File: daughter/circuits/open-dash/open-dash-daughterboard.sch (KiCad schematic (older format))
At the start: 13 parts, among them J1 Conn_01x01_Female, J2 Conn_01x01_Female, J3 Conn_01x01_Female, J4 Conn_01x01_Female, J43 Conn_02x02_Counter_Clockwise, J5 Conn_02x06_Odd_Even, J6 Conn_IDE_40, J7 Conn_IDE_40, J8 Conn_IDE_40, Q40 Q_AO3401A

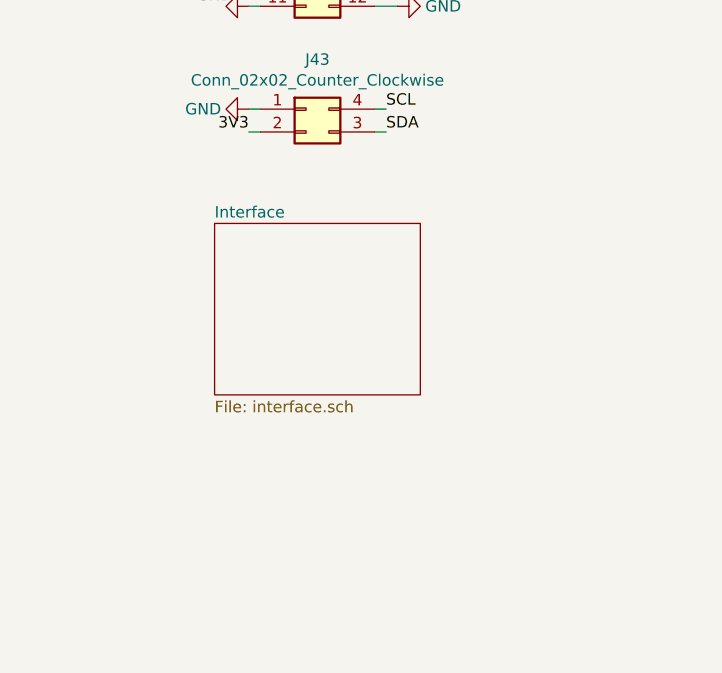
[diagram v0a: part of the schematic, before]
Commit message: send v1.4 to board house. Corrected source-drain on fets.
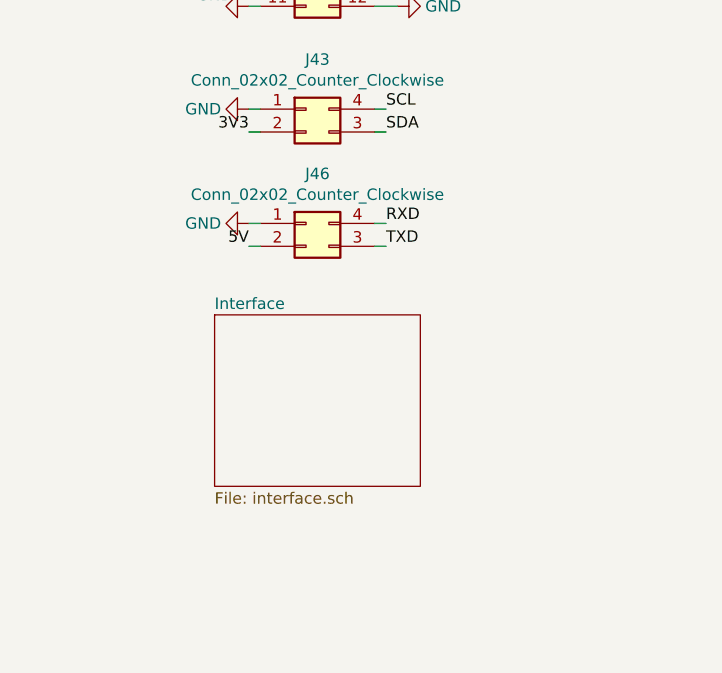
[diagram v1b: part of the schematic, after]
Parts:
- added J46: Conn_02x02_Counter_Clockwise, Connector_PinHeader_2.54mm:PinHeader_2x02_P2.54mm_Vertical_SMD, symbol open-dash-daughterboard-rescue:Conn_02x02_Counter_Clockwise-Connector_Generic
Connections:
- net 5V: now also J46.2 (Pin_2)
- net GND: now also J46.1 (Pin_1)
- net RXD: now also J46.4 (Pin_4)
- net TXD: now also J46.3 (Pin_3)
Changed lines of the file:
@@
 	1450 4700 1500 4700
 $Sheet
-S 1300 5850 900  750
+S 1300 6250 900  750
 U 657571BE
 F0 "Interface" 50
@@
 	-1   0    0    1
 $EndComp
+$Comp
+L open-dash-daughterboard-rescue:Conn_02x02_Counter_Clockwise-Connector_Generic J?
+U 1 1 621B051F
+P 1700 5850
+AR Path="/60DDD162/621B051F" Ref="J?"  Part="1"
+AR Path="/621B051F" Ref="J46"  Part="1"
+F 0 "J46" H 1750 6067 50  0000 C CNN
+F 1 "Conn_02x02_Counter_Clockwise" H 1750 5976 50  0000 C CNN
+F 2 "Connector_PinHeader_2.54mm:PinHeader_2x02_P2.54mm_Vertical_SMD" H 1700 5850 50  0001 C CNN
+F 3 "~" H 1700 5850 50  0001 C CNN
+	1    1700 5850
+	1    0    0    -1
+$EndComp
+$Comp
+L open-dash-daughterboard-rescue:GND-power #PWR?
+U 1 1 621B077D
+P 1450 5850
+AR Path="/5ABD187E/621B077D" Ref="#PWR?"  Part="1"
+AR Path="/621B077D" Ref="#PWR0177"  Part="1"
+AR Path="/5A7BADB8/621B077D" Ref="#PWR?"  Part="1"
+AR Path="/60DDD162/621B077D" Ref="#PWR?"  Part="1"
+F 0 "#PWR0177" H 1450 5600 50  0001 C CNN
+F 1 "GND" V 1450 5650 50  0000 C CNN
+F 2 "" H 1450 5850 50  0000 C CNN
+F 3 "" H 1450 5850 50  0000 C CNN
+	1    1450 5850
+	0    1    1    0
+$EndComp
+Wire Wire Line
+	1450 5850 1500 5850
+Wire Wire Line
+	1450 5950 1500 5950
+Text Label 2050 5950 0    50   ~ 0
+TXD
+Text Label 2050 5850 0    50   ~ 0
+RXD
+Wire Wire Line
+	2000 5850 2050 5850
+Wire Wire Line
+	2050 5950 2000 5950
+Text Label 1450 5950 2    50   ~ 0
+5V
 $EndSCHEMATC
